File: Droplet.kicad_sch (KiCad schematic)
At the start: 15 parts, among them J1 Conn_01x05, J2 Conn_01x05, J3 Prog, U1 ATtiny202-SS, U2 IRM-H6xxT

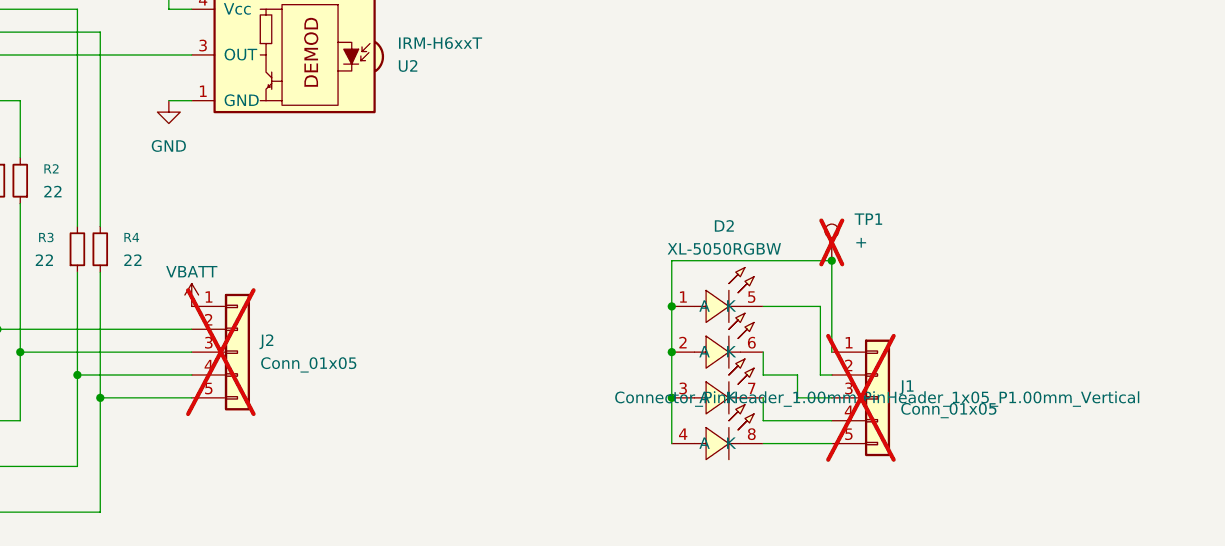
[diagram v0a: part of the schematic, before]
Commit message: do layout, including mouse bites
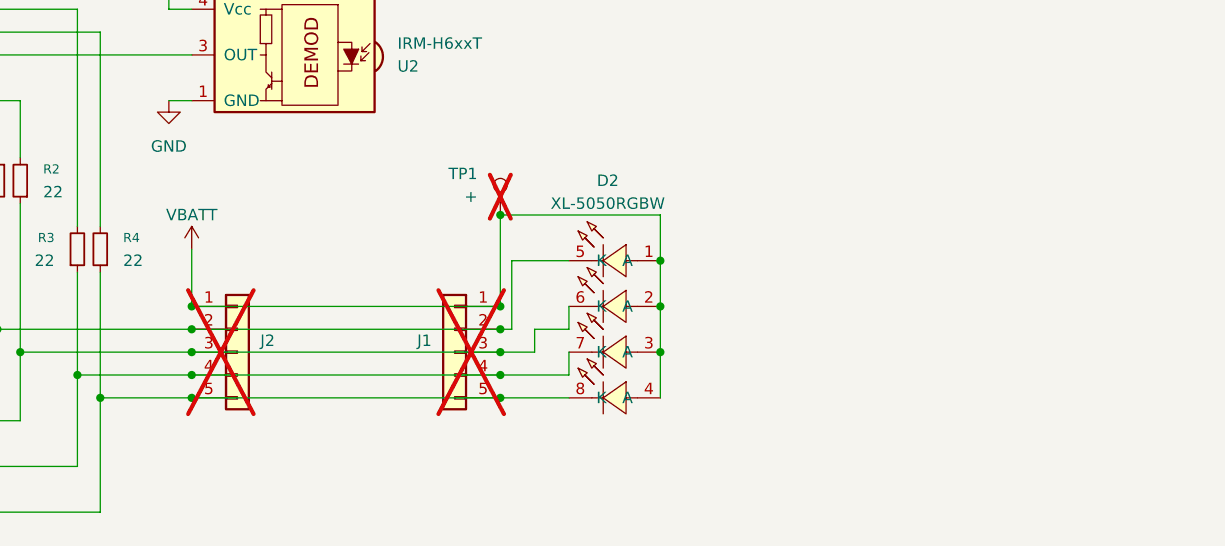
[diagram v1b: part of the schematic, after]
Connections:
- net VBATT: now also D2.1 (A), D2.2 (A), D2.3 (A), D2.4 (A), J1.1 (Pin_1), TP1.1
- net at D1.7 (K), J2.4 (Pin_4), R3.1: now also D2.7 (K), J1.4 (Pin_4)
- net at D1.8 (K), J2.5 (Pin_5), R4.1: now also D2.8 (K), J1.5 (Pin_5)
- net at D1.5 (K), J2.2 (Pin_2), R1.2: now also D2.5 (K), J1.2 (Pin_2)
- net at D1.6 (K), J2.3 (Pin_3), R2.1: now also D2.6 (K), J1.3 (Pin_3)
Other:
- moved on the sheet: D2, J1, TP1

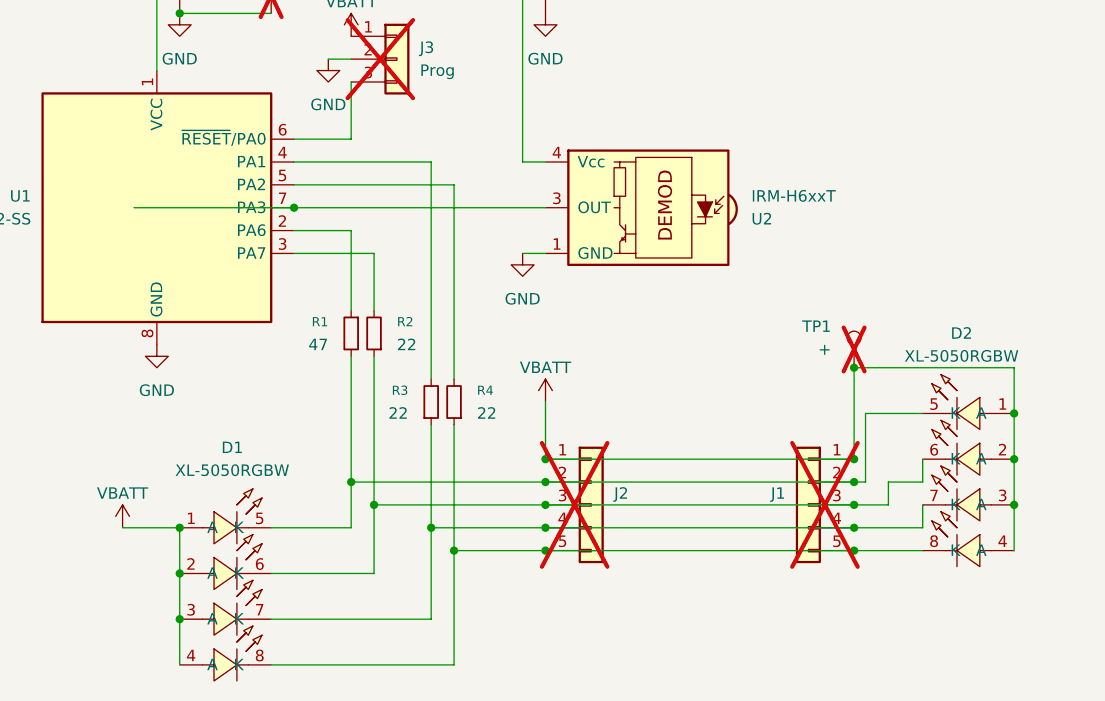
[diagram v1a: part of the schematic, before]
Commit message: update to use warm white RGB LED. Single unit layout
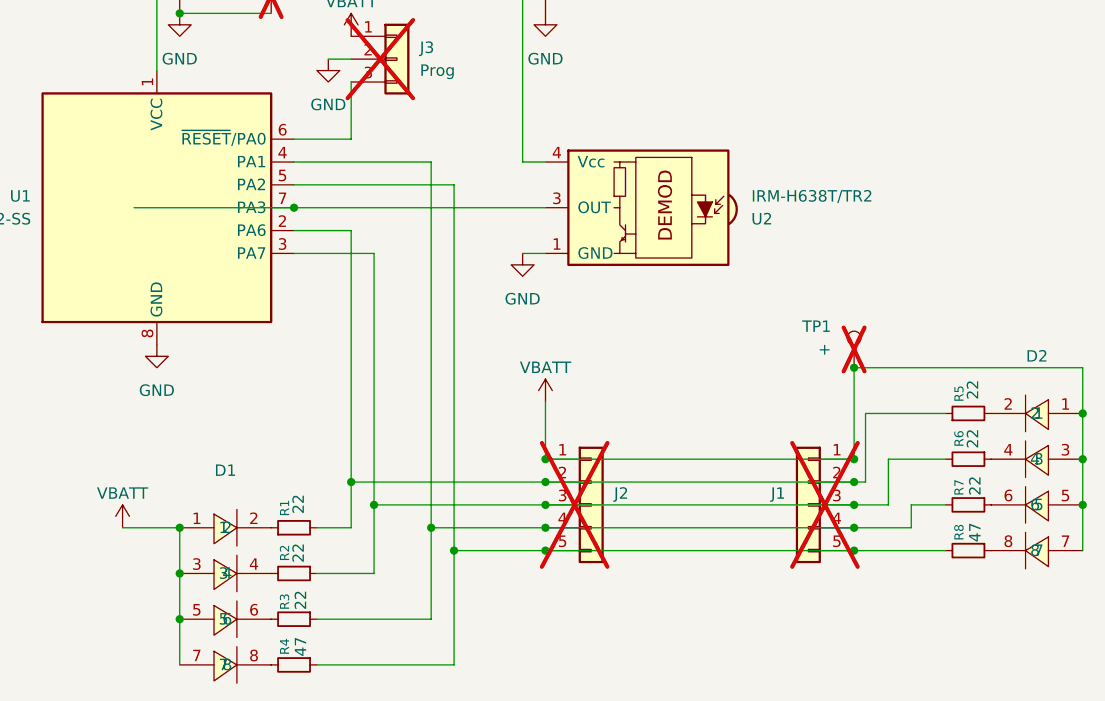
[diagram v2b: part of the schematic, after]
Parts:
- removed D1, D2: XL-5050RGBW, EasyEDA-Imports:LED-SMD_8P-L5.0-W5.0-P1.32-TL, symbol EasyEDA-Imports:XL-5050RGBW
- added D1, D2: HL-5050RGBW-S1-A27, easyeda2kicad:LED-SMD_8P-L5.0-W5.0-P1.20_HL-5050RGBW-S1-A27, symbol easyeda2kicad:HL-5050RGBW-S1-A27
- added R5, R6, R7: 22, Resistor_SMD:R_0402_1005Metric, symbol Device:R_Small
- added R8: 47, Resistor_SMD:R_0402_1005Metric, symbol Device:R_Small
- R1: value 47 -> 22
- R4: value 22 -> 47
- U2: value IRM-H6xxT -> IRM-H638T/TR2
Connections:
- net VBATT: now also D1.1, D1.3, D1.5, D1.7, D2.1, D2.3, D2.5, D2.7
- net at J1.4 (Pin_4), J2.4 (Pin_4), R3.1: now also U1.4 (PA1), R7.2
- net at R3.2: now also D1.6; no longer U1.4 (PA1)
- net at J1.5 (Pin_5), J2.5 (Pin_5), R4.1: now also U1.5 (PA2), R8.2
- net at R4.2: now also D1.8; no longer U1.5 (PA2)
- net at R1.1: now also D1.2; no longer U1.2 (PA6)
- net at R2.2: now also D1.4; no longer U1.3 (PA7)
- net at J1.2 (Pin_2), J2.2 (Pin_2), R1.2: now also U1.2 (PA6), R5.1
- net at J1.3 (Pin_3), J2.3 (Pin_3), R2.1: now also U1.3 (PA7), R6.2
- new net: D2.2, R5.2
- new net: D2.8, R8.1
- new net: D2.6, R7.1
- new net: D2.4, R6.1
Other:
- moved on the sheet: R1, R2, R3, R4

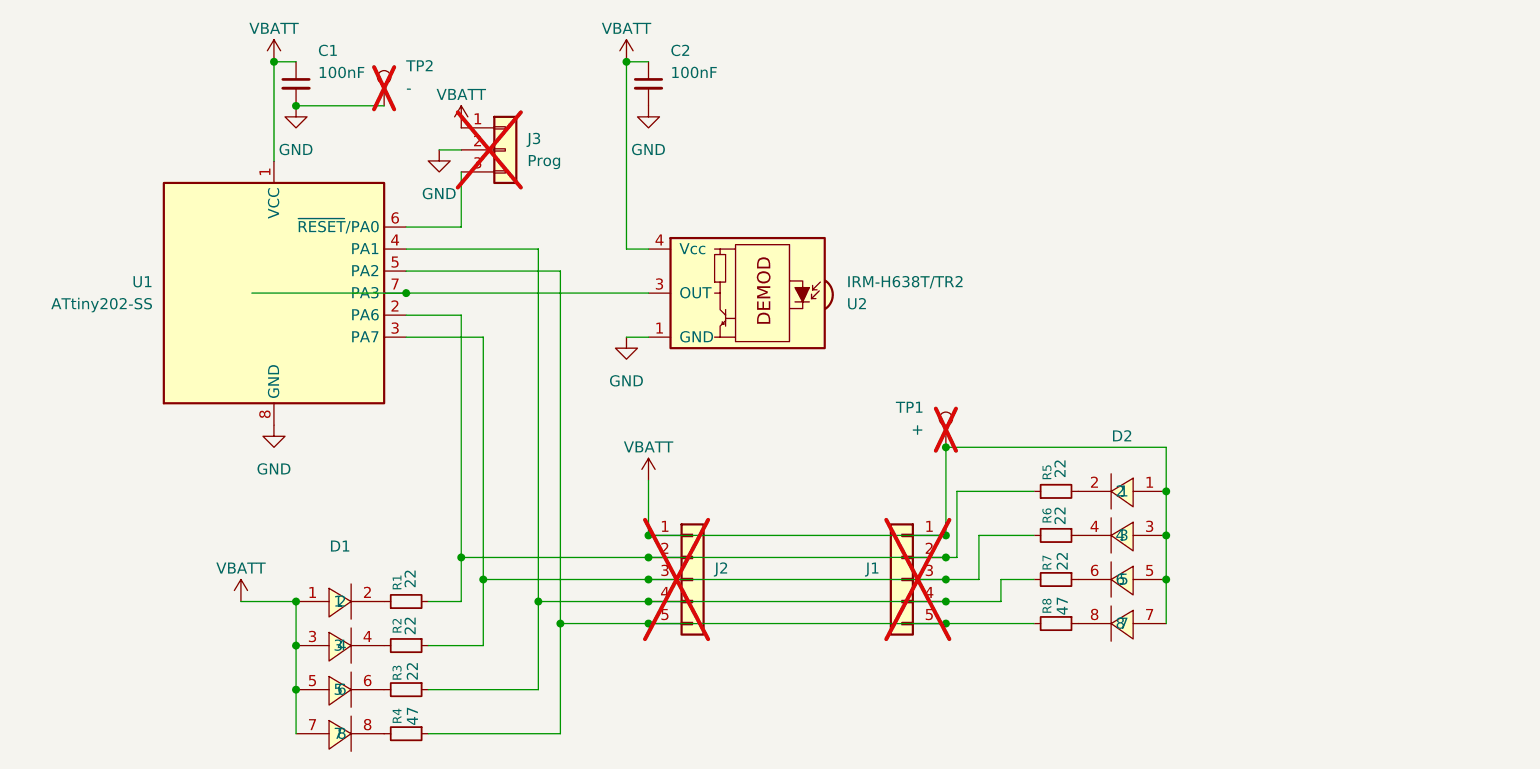
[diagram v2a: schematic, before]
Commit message: rework with castellated connectors
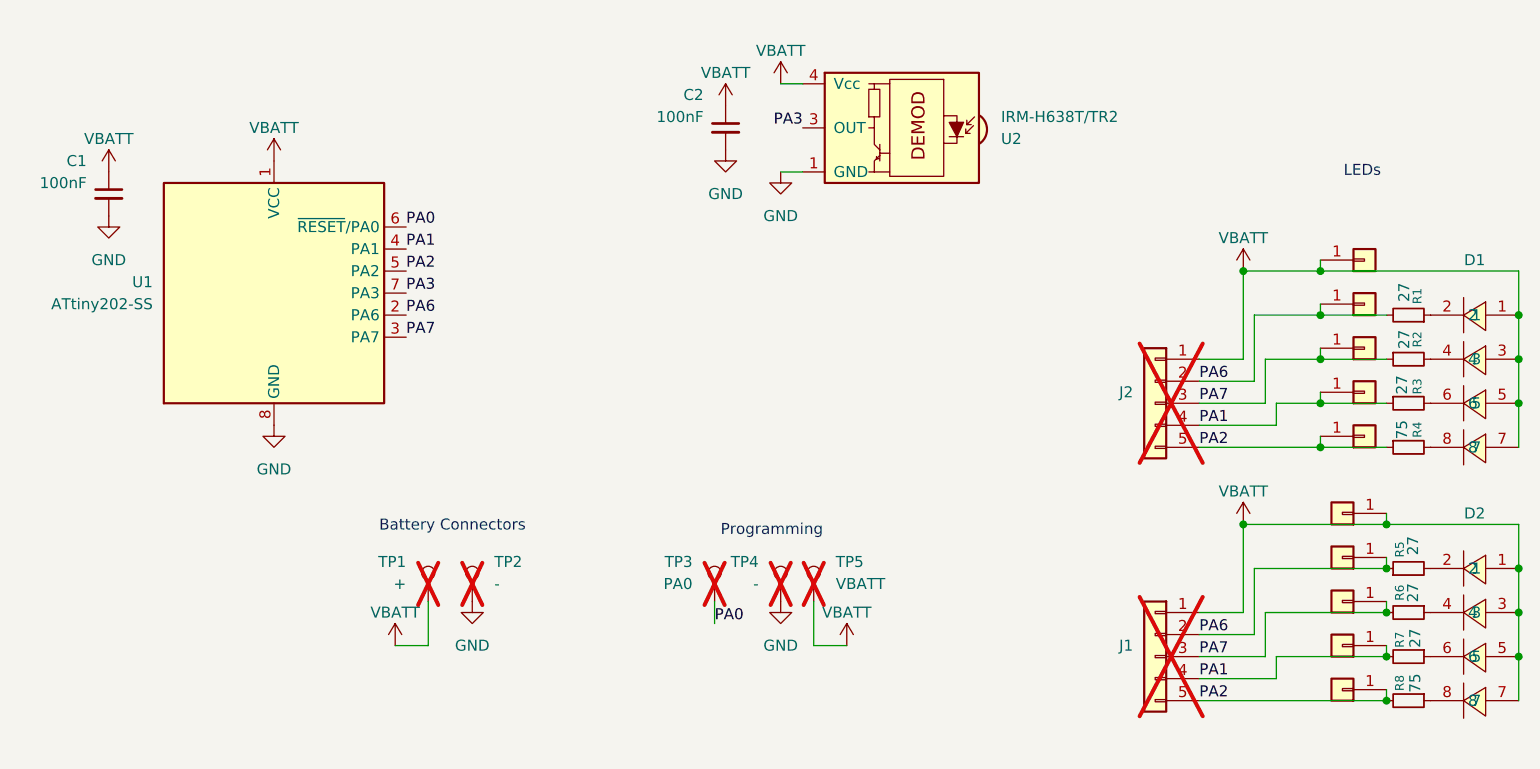
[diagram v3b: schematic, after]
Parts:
- removed J3: Prog, Connector_PinHeader_1.00mm:PinHeader_1x03_P1.00mm_Vertical, symbol Connector_Generic:Conn_01x03
- added J10, J11, J12, J3, J4, J5, J6, J7, J8, J9: Conn_01x01, Custom:1x01_P2.54mm castellated, symbol Connector_Generic:Conn_01x01
- added TP3: PA0, TestPoint:TestPoint_Pad_D1.5mm, symbol Connector:TestPoint
- added TP4: -, TestPoint:TestPoint_Pad_D1.5mm, symbol Connector:TestPoint
- added TP5: VBATT, TestPoint:TestPoint_Pad_D1.5mm, symbol Connector:TestPoint
- R1, R2, R3, R5, R6, R7: value 22 -> 27
- R4, R8: value 47 -> 75
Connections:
- net GND: now also TP4.1
- net VBATT: now also J12.1 (Pin_1), J7.1 (Pin_1), TP5.1
- net PA1: now reaches J1.4 (Pin_4), J2.4 (Pin_4), R3.1, R7.2, U1.4 (PA1)
- net PA1: now also J5.1 (Pin_1), J9.1 (Pin_1)
- net PA6: now reaches J1.2 (Pin_2), J2.2 (Pin_2), R1.2, R5.1, U1.2 (PA6)
- net PA6: now also J11.1 (Pin_1), J3.1 (Pin_1)
- net PA2: now reaches J1.5 (Pin_5), J2.5 (Pin_5), R4.1, R8.2, U1.5 (PA2)
- net PA2: now also J6.1 (Pin_1), J8.1 (Pin_1)
- net PA7: now reaches J1.3 (Pin_3), J2.3 (Pin_3), R2.1, R6.2, U1.3 (PA7)
- net PA7: now also J10.1 (Pin_1), J4.1 (Pin_1)
- net PA0: now reaches U1.6 (~{RESET}/PA0)
- net PA0: now also TP3.1
- net PA3: now reaches U1.7 (PA3), U2.3 (OUT)
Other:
- note added: "Battery Connectors"
- note added: "LEDs"
- note added: "Programming"
- moved on the sheet: C1, C2, D1, D2, J1, J2, R1, R2, R3, R4, R5, R6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

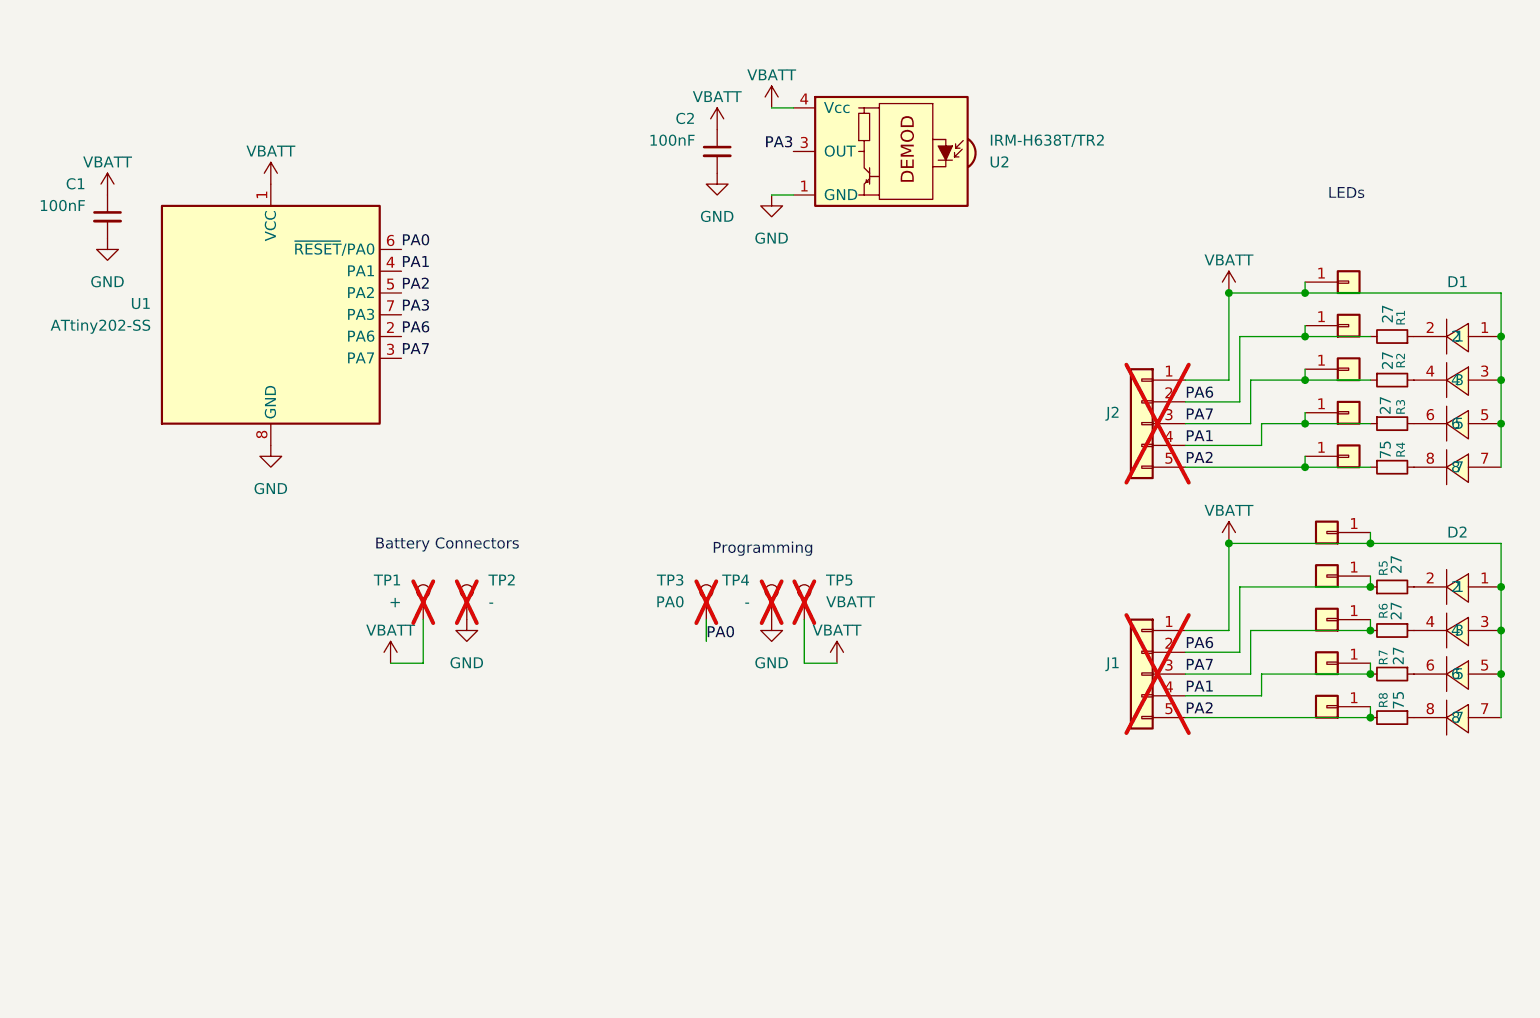
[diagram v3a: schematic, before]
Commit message: update schematic readability, rotate ir receiver
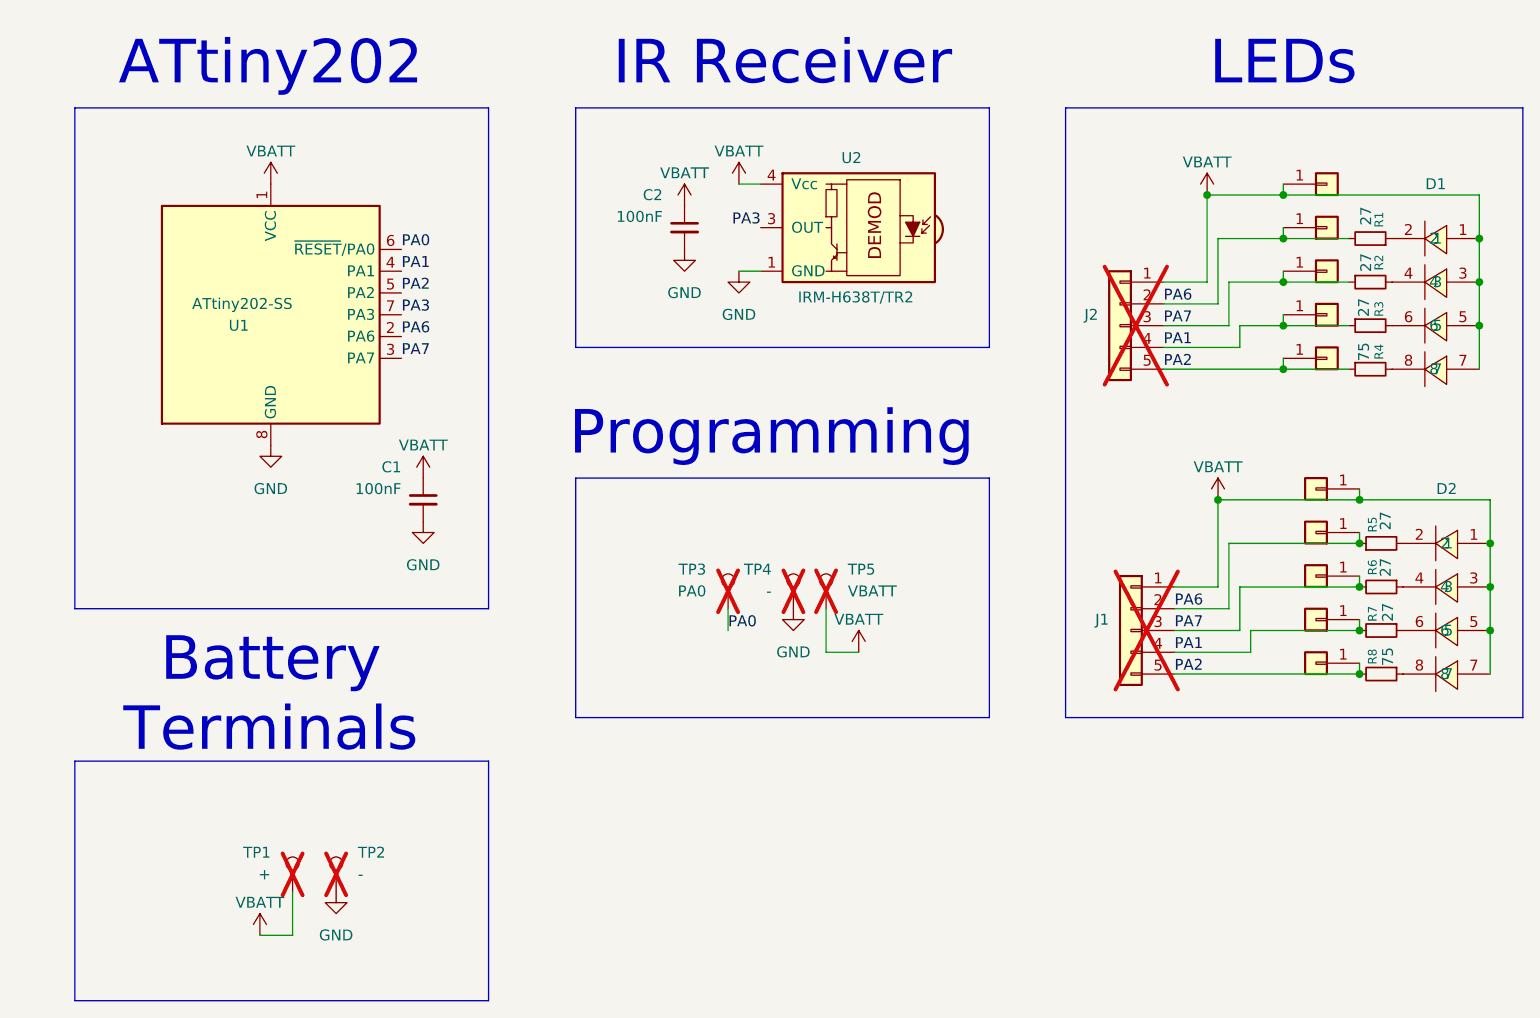
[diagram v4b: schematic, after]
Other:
- note added: "ATtiny202"
- note added: "Battery Terminals"
- note added: "IR Receiver"
- note removed: "Battery Connectors"
- moved on the sheet: C1, C2, D1, D2, J1, J2, R1, R2, R3, R4, R5, R6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
